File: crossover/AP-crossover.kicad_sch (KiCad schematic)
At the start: 91 parts, among them U1 OPA1604, U2 OPA1604, U3 LM317_TO-252, U4 LM337_TO252

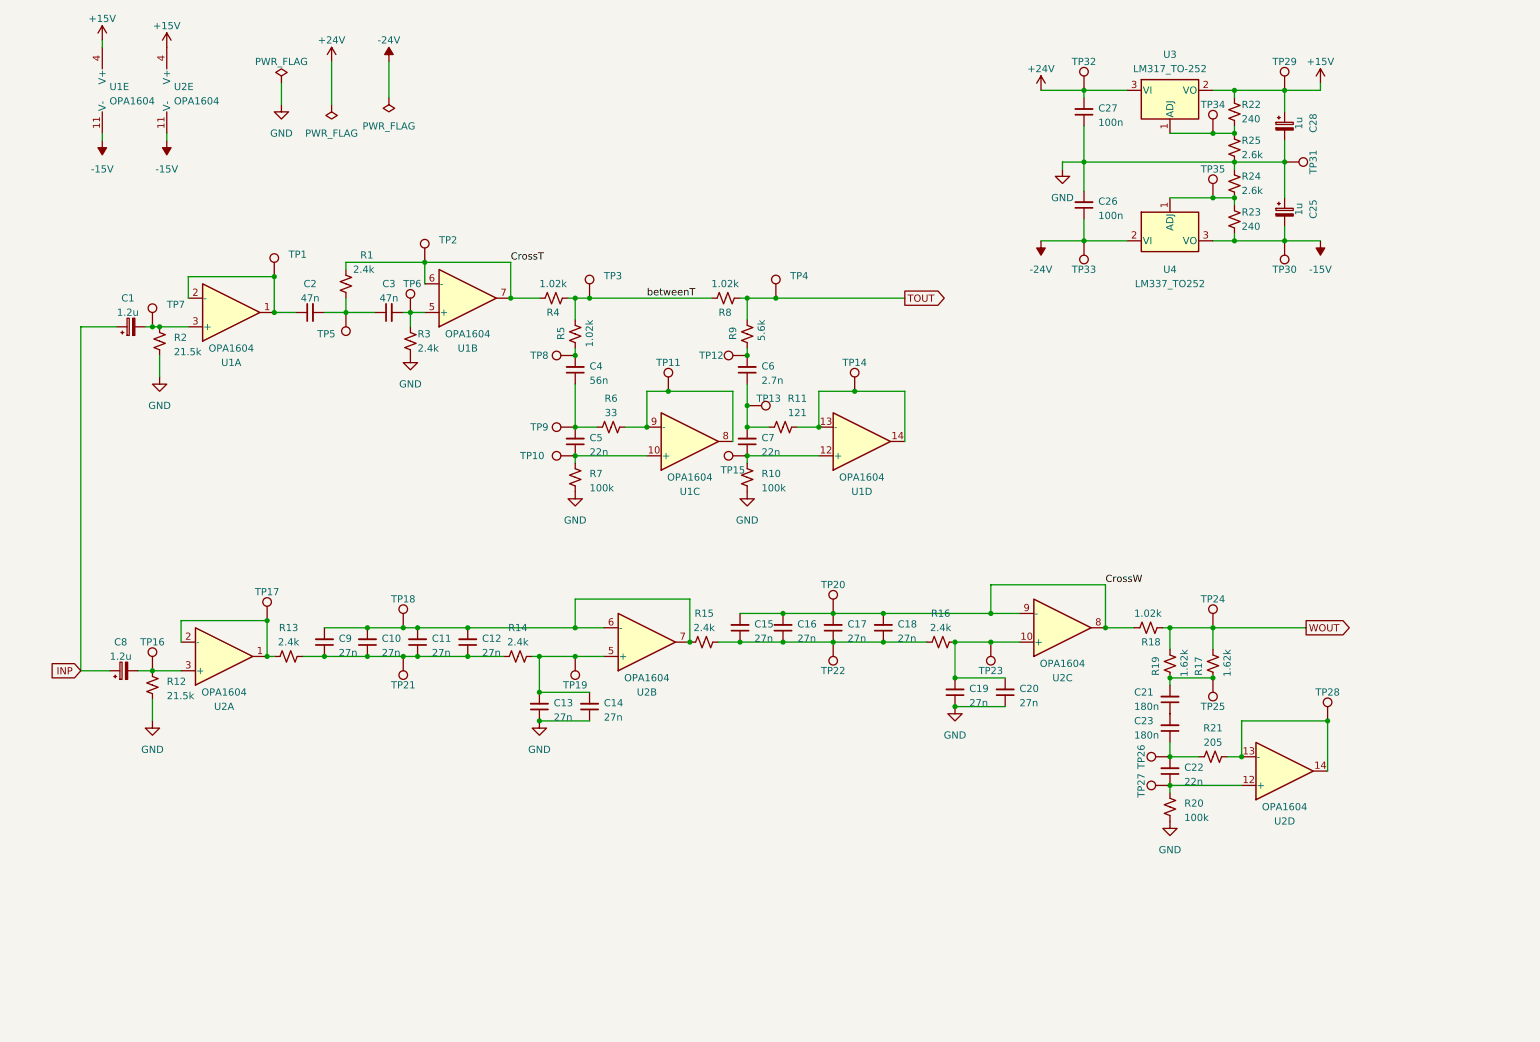
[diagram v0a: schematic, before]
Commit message: Update pcb layout to revision B, add balanced input
Co-Authored-By: ithinkido <52834821+ithinkido@users.noreply.github.com>
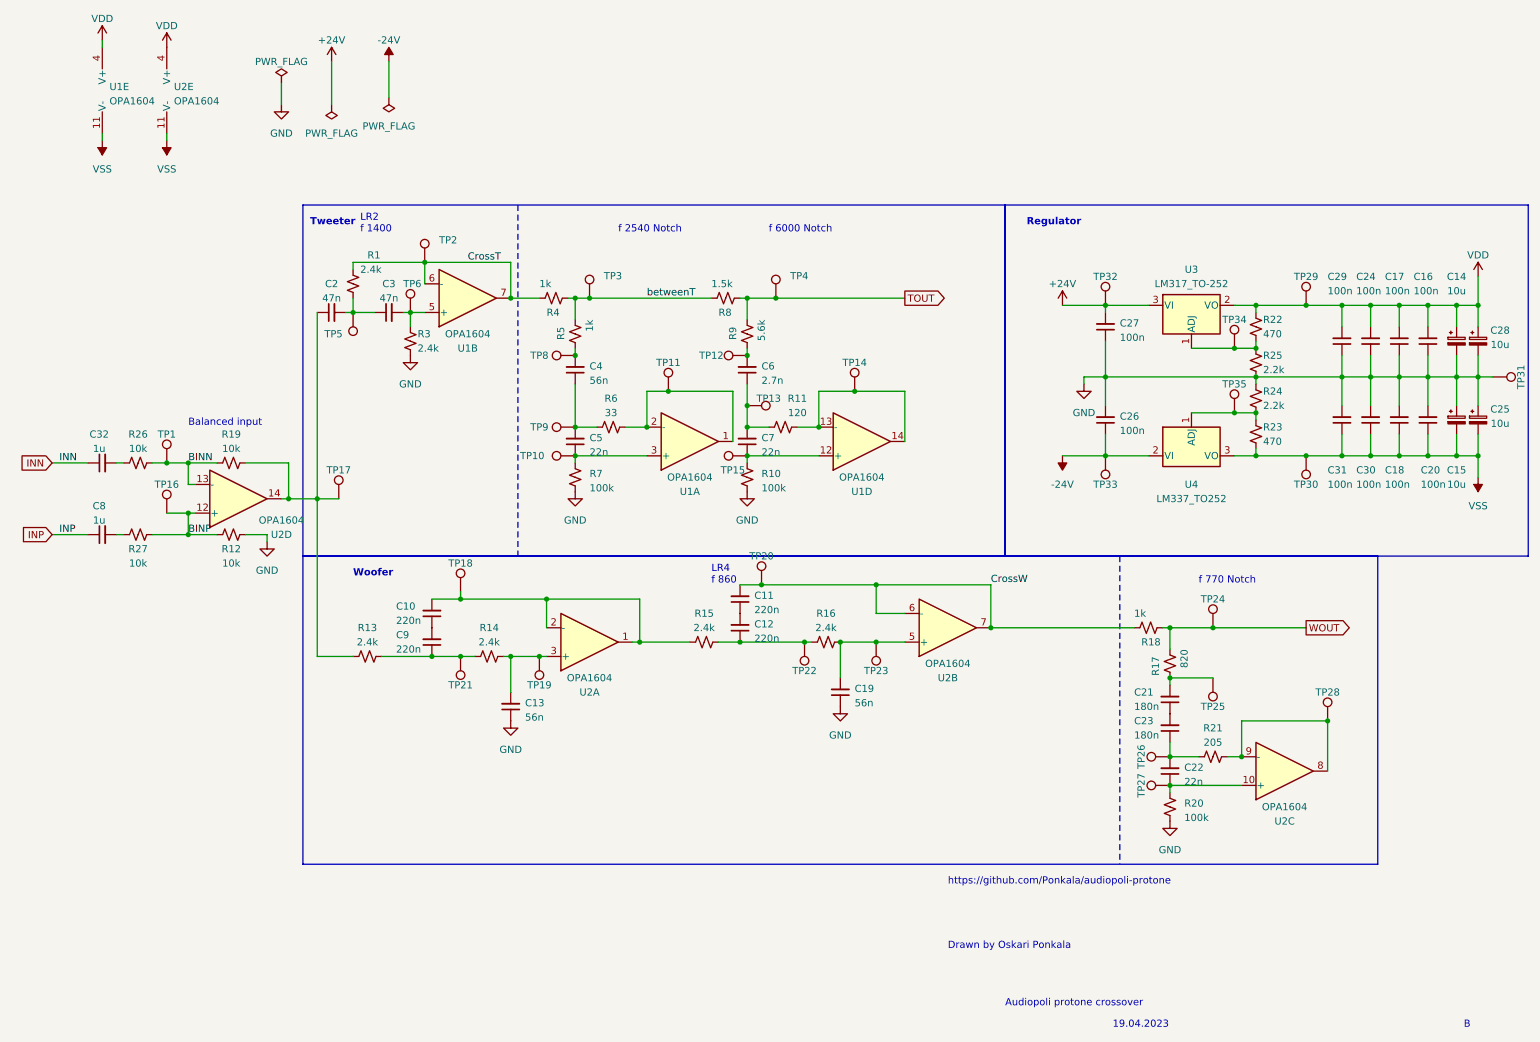
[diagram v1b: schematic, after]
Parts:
- removed C1: 1.2u, Capacitor_SMD:CP_Elec_5x5.7, symbol Device:C_Polarized_Small
- removed C14, C15: 27n, Capacitor_SMD:C_0603_1608Metric, symbol Device:C_Small
- removed R2: 21.5k, Resistor_SMD:R_0805_2012Metric, symbol Device:R_Small_US
- removed TP7: TestPoint, TestPoint:TestPoint_THTPad_D1.0mm_Drill0.5mm, symbol Connector:TestPoint
- removed unit 3 of U1
- added C14, C15: 10u, Capacitor_SMD:CP_Elec_5x5.4, symbol Device:C_Polarized_Small
- added C24, C29, C30, C31: 100n, Capacitor_SMD:C_0805_2012Metric, symbol Device:C_Small
- added C32: 1u, Capacitor_SMD:C_0805_2012Metric, symbol Device:C_Small
- added R26, R27: 10k, Resistor_SMD:R_0603_1608Metric, symbol Device:R_Small_US
- C10, C11, C12, C9: value 27n -> 220n
- C13, C19: value 27n -> 56n
- C16, C17, C18, C20: value 27n -> 100n; footprint Capacitor_SMD:C_0603_1608Metric -> Capacitor_SMD:C_0805_2012Metric
- C2, C3, C6: footprint Capacitor_SMD:C_0805_2012Metric -> Capacitor_SMD:C_0603_1608Metric
- C25, C28: value 1u -> 10u; footprint Capacitor_SMD:CP_Elec_4x5.4 -> Capacitor_SMD:CP_Elec_5x5.4
- C4: footprint Capacitor_SMD:C_1206_3216Metric -> Capacitor_SMD:C_0603_1608Metric
- C8: value 1.2u -> 1u; footprint Capacitor_SMD:CP_Elec_5x5.7 -> Capacitor_SMD:C_0805_2012Metric; symbol Device:C_Polarized_Small -> Device:C_Small
- R10, R20, R7: footprint Resistor_SMD:R_1206_3216Metric -> Resistor_SMD:R_0603_1608Metric
- R11: value 121 -> 120; footprint Resistor_SMD:R_1206_3216Metric -> Resistor_SMD:R_0603_1608Metric
- R12: value 21.5k -> 10k; footprint Resistor_SMD:R_0805_2012Metric -> Resistor_SMD:R_0603_1608Metric
- R17: value 1.62k -> 820
- R18, R4, R5: value 1.02k -> 1k; footprint Resistor_SMD:R_1206_3216Metric -> Resistor_SMD:R_0603_1608Metric
- R19: value 1.62k -> 10k
- R22, R23: value 240 -> 470; footprint Resistor_SMD:R_2010_5025Metric -> Resistor_SMD:R_0805_2012Metric
- R24, R25: value 2.6k -> 2.2k; footprint Resistor_SMD:R_1210_3225Metric -> Resistor_SMD:R_0805_2012Metric
- R8: value 1.02k -> 1.5k; footprint Resistor_SMD:R_1206_3216Metric -> Resistor_SMD:R_0603_1608Metric
- R9: footprint Resistor_SMD:R_0805_2012Metric -> Resistor_SMD:R_0603_1608Metric
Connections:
- net CrossW: now also C11.2, U2.6 (-), U2.7; no longer C16.2, C17.2, C18.2, U2.8, U2.9 (-)
- net GND: now also C16.1, C17.1, C18.2, C20.2, C14.2, C15.1, C24.1, C29.1, C30.2, C31.2; no longer C20.1
- net WOUT: no longer R19.2
- net at C22.1, R20.2, TP27.1: now also U2.10 (+); no longer U2.12 (+)
- net at R21.2, TP28.1: now also U2.8, U2.9 (-); no longer U2.13 (-), U2.14
- net at C9.1, R13.1, R14.2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: no longer C10.1, C11.1, C12.1
- net at U1.3 (+): now also C5.1, R7.2, TP10.1
- net at U1.1, U1.2 (-): now also R6.2, TP11.1; no longer C2.1, TP1.1
- net at C21.2, R17.1, TP25.1: no longer R19.1
- net at C13.2, R14.1, TP19.1: now also U2.3 (+); no longer U2.5 (+)
- net at R15.1, R16.2, TP22.1: now also C12.1; no longer C16.1, C17.1, C18.1
- net at C19.2, R16.1, TP23.1: now also U2.5 (+); no longer C20.2, U2.10 (+)
- net at R13.2, TP17.1: now also C2.1, R19.2, U2.14; no longer U2.1, U2.2 (-)
- net BINP: now reaches R12.1, TP16.1
- net BINP: now also U2.12 (+), R27.2; no longer C8.2, U2.3 (+)
- net +15V renamed VDD
- net VDD: now also C16.2, C17.2, C14.1, C24.2, C29.2
- net -15V renamed VSS
- net VSS: now also C18.1, C20.1, C15.2, C30.1, C31.1
- new net: C10.1, C9.2
- new net: C10.2, R15.2, TP18.1, U2.1, U2.2 (-)
- new net: C11.1, C12.2
- new net: C32.2, R26.2
- new net: C8.2, R27.1
- new net BINN: R19.1, R26.1, TP1.1, U2.13 (-)
- new net INN: C32.1
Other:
- note added: "19.04.2023"
- note added: "Audiopoli protone crossover"
- note added: "B"
- note added: "Balanced input"
- note added: "Drawn by Oskari Ponkala"
- note added: "LR2 f 1400"
- note added: "LR4 f 860"
- note added: "Regulator"
- note added: "Tweeter"
- note added: "Woofer"
- note added: "f 2540 Notch"
- note added: "f 6000 Notch"
- note added: "f 770 Notch"
- note added: "https://github.com/Ponkala/audiopoli-protone"
- moved on the sheet: C13, C19, C2, C25, C26, C27, C28, C9, R1, R13, R14, R16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

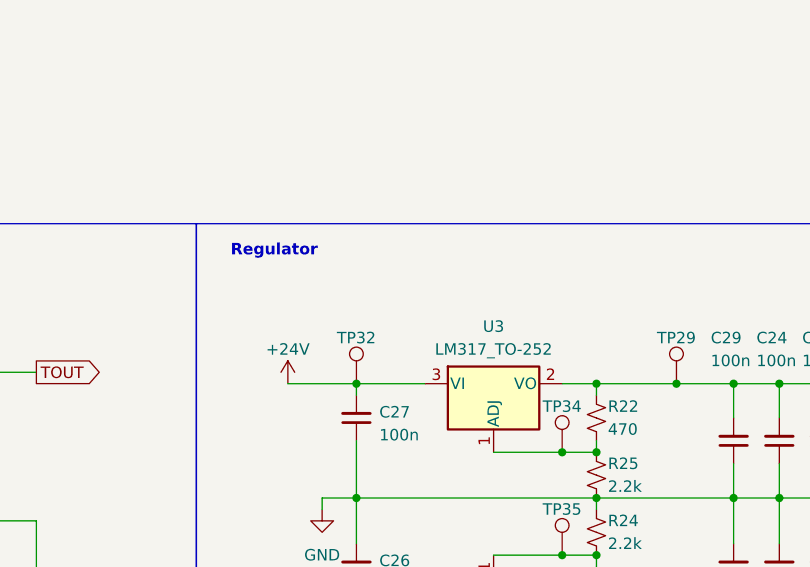
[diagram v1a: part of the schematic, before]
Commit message: Add regulator voltage levels
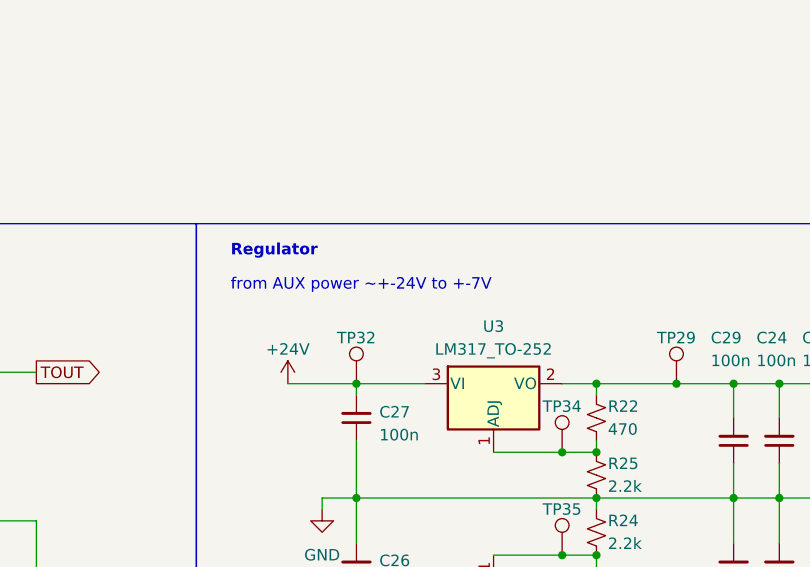
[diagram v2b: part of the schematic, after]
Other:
- note added: "from AUX power ~+-24V to +-7V"
